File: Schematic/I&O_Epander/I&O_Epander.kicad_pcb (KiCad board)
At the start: 2 copper layers, 203.2 x 50.8 mm, 73 parts, among them J1 RJ45-Unshielded, J10 RJ45-Unshielded, J11 RJ45-Unshielded, J12 KLDVHCX-0202-A, J13 RJ45-Unshielded, J14 RJ45-Unshielded, J2 RJ45-Unshielded, J3 RJ45-Unshielded, J4 RJ45-Unshielded, J5 RJ45-Unshielded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

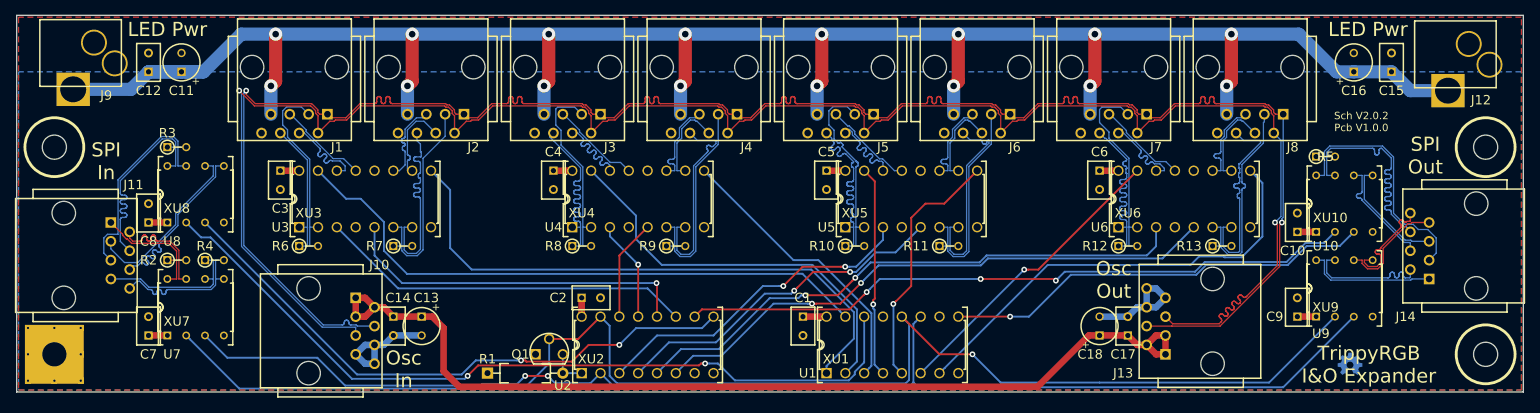
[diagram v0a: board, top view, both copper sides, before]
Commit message: KiCAD upgrade
Upgrade schematic and pcb files for KiCad v5.
Make 8-pin dip holes larger for crimped-pin sockets
InteractiveBOM plugin v1.1 board stuffing files generated.
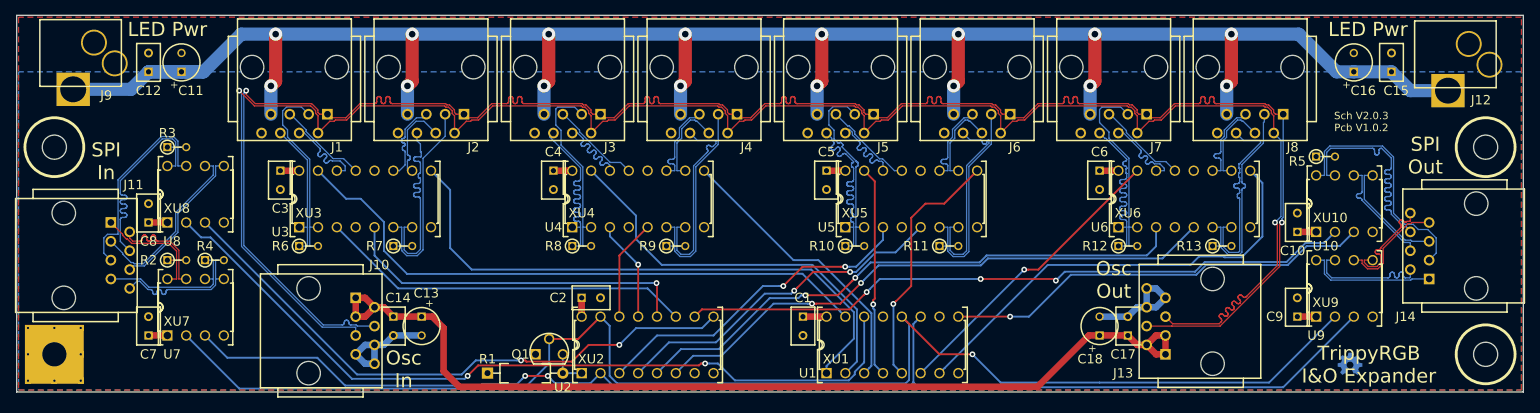
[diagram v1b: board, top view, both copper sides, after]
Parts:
- moved C13 1.27 mm to (92.7, 130.8)
- moved C18 1.27 mm to (184.2, 130.8)
- moved C11 1.27 mm to (60.3, 95.2)
- moved C16 1.27 mm to (218.4, 95.2)
- turned U1 to 90 degrees
- turned U10 to 90 degrees
- turned U2 to 90 degrees
- turned U3 to 90 degrees
- turned U4 to 90 degrees
- turned U5 to 90 degrees
- turned U6 to 90 degrees
- turned U7 to 90 degrees
- turned U8 to 90 degrees
- turned U9 to 90 degrees
- turned XU1 to 90 degrees
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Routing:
- net /MISO-: track 23.8 -> 20.8 mm
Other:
- rule pad_to_mask_clearance: 0 -> 0.0508
- board text added: "Sch V2.0.3 Pcb V1.0.2"
- board text removed: "Sch V2.0.2 Pcb V1.0.0"
